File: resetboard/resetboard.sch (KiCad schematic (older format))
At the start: 24 parts, among them J1 USB_C_Receptacle_USB2.0, J2 Conn_02x20_Odd_Even, J3 Conn_01x02, J4 Conn_01x06, SW1 SW_SPST, U1 PCF8523TK, U2 SE050, Y1 Crystal_Small

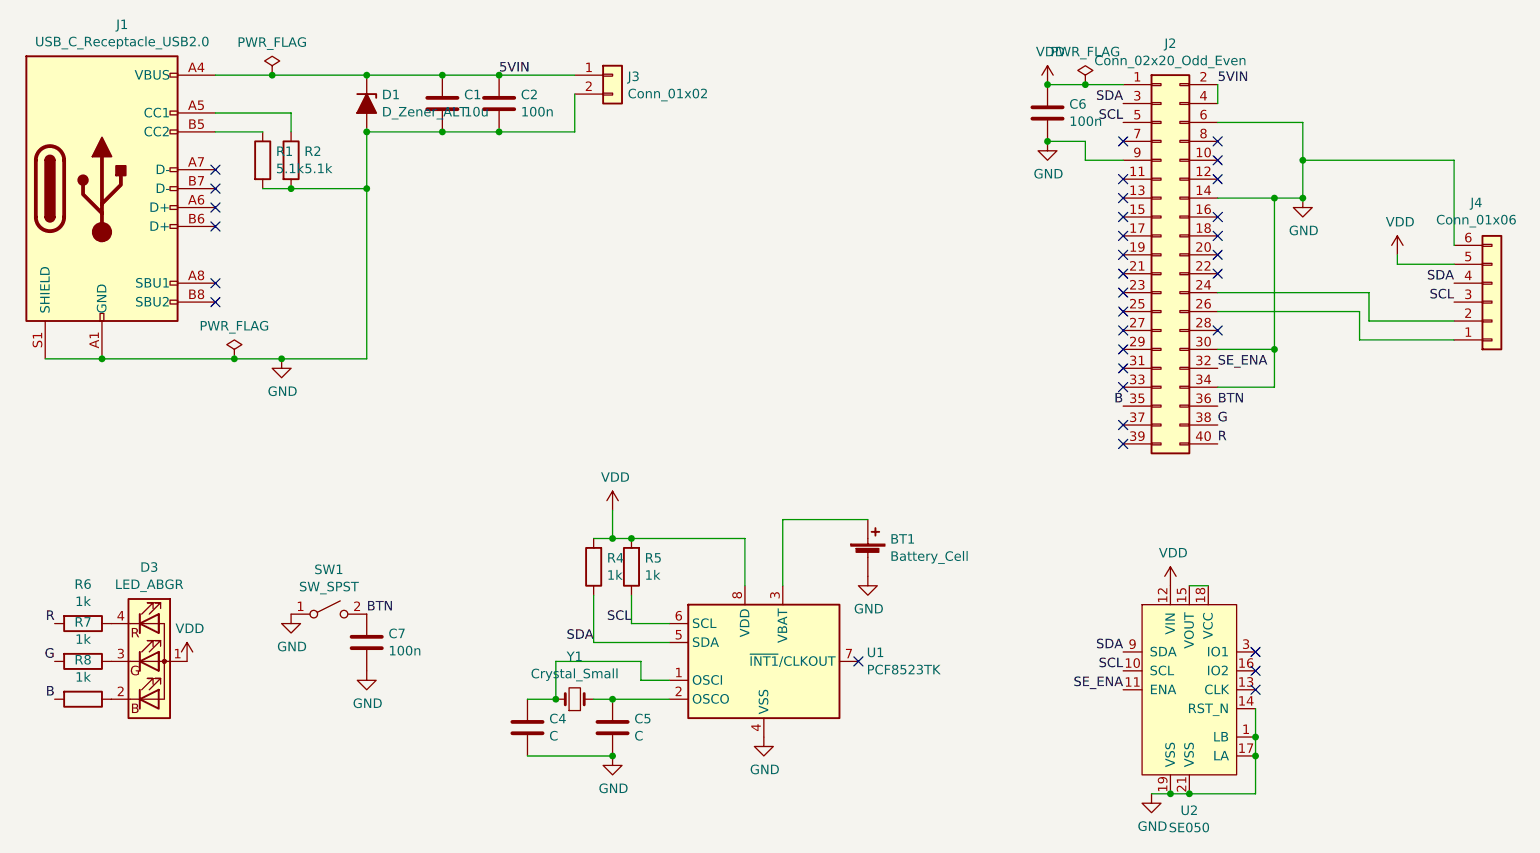
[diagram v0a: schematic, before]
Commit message: Remove ziptie holes Add filtering to RTC supply Add NFET-controlled fan on GPIO18 Switch fan connector to horizontal Rearrange parts to move fan connector to left edge of board Rotate LED towards edge Relabel R and B channels of RGB LED to match part Add vendor STEP model for RGB LED Regenerate STEP file
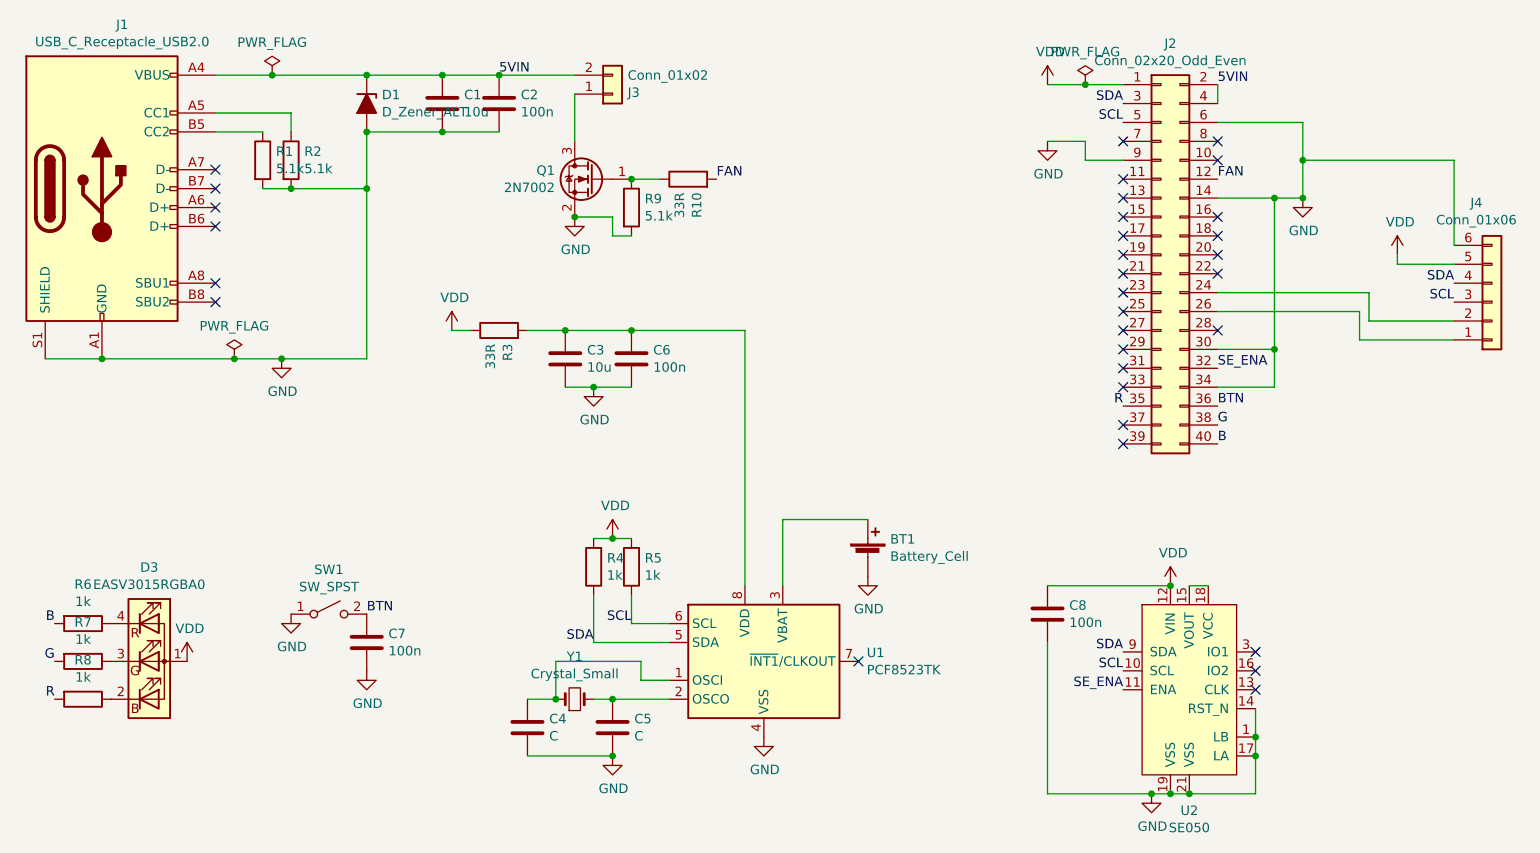
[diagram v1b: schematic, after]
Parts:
- added C3: 10u, Capacitor_SMD:C_0805_2012Metric, symbol Device:C
- added C8: 100n, Capacitor_SMD:C_0603_1608Metric, symbol Device:C
- added Q1: 2N7002, Package_TO_SOT_SMD:SOT-23, symbol Transistor_FET:2N7002
- added R10, R3: 33R, Resistor_SMD:R_0603_1608Metric, symbol Device:R
- added R9: 5.1k, Resistor_SMD:R_0603_1608Metric, symbol Device:R
- D3: value LED_ABGR -> EASV3015RGBA0
- J3: footprint Connector_JST:JST_GH_BM02B-GHS-TBT_1x02-1MP_P1.25mm_Vertical -> Connector_JST:JST_GH_SM02B-GHS-TB_1x02-1MP_P1.25mm_Horizontal
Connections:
- net 5VIN: now also J3.2 (Pin_2); no longer J3.1 (Pin_1)
- net B: now also J2.40 (Pin_40), R6.2; no longer J2.35 (Pin_35), R8.2
- net GND: now also C3.2, C8.2, Q1.2 (S), R9.2; no longer J3.2 (Pin_2)
- net R: now also J2.35 (Pin_35), R8.2; no longer J2.40 (Pin_40), R6.2
- net VDD: now also C8.1, R3.1; no longer C6.1, U1.8 (VDD)
- net FAN: now reaches J2.12 (Pin_12)
- net FAN: now also R10.2
- new net: C3.1, C6.1, R3.2, U1.8 (VDD)
- new net: J3.1 (Pin_1), Q1.3 (D)
- new net: Q1.1 (G), R10.1, R9.1
- no-connect marks 33 -> 32
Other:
- moved on the sheet: C6
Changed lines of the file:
@@
 P 3100 5300
 F 0 "D3" H 3100 5797 50  0000 C CNN
-F 1 "LED_ABGR" H 3100 5706 50  0000 C CNN
+F 1 "EASV3015RGBA0" H 3100 5706 50  0000 C CNN
 F 2 "catwsparts:HQ12-2353RBGC" H 3100 5250 50  0001 C CNN
 F 3 "~" H 3100 5250 50  0001 C CNN
@@
 Wire Wire Line
 	5450 5200 5450 4950
-Wire Wire Line
-	5450 4650 5550 4650
-Connection ~ 5550 4650
-Wire Wire Line
-	5550 4650 5650 4650
-$Comp
-L power:VDD #PWR0103
-U 1 1 5FC4EE71
-P 5550 4500
-F 0 "#PWR0103" H 5550 4350 50  0001 C CNN
-F 1 "VDD" H 5565 4673 50  0000 C CNN
-F 2 "" H 5550 4500 50  0001 C CNN
-F 3 "" H 5550 4500 50  0001 C CNN
-	1    5550 4500
-	1    0    0    -1
-$EndComp
 $Comp
 L power:VDD #PWR0104
@@
 $EndComp
 Connection ~ 9200 2850
-Text Label 8750 4150 0    50   ~ 0
+Text Label 8250 3950 2    50   ~ 0
 R
 Text Label 8750 4050 0    50   ~ 0
 G
-Text Label 8250 3950 2    50   ~ 0
+Text Label 8750 4150 0    50   ~ 0
 B
 $Comp
@@
 Text Label 4250 5050 0    50   ~ 0
 BTN
-Text Label 2600 5100 2    50   ~ 0
+Text Label 2600 5500 2    50   ~ 0
 R
 Text Label 2600 5300 2    50   ~ 0
 G
-Text Label 2600 5500 2    50   ~ 0
+Text Label 2600 5100 2    50   ~ 0
 B
 $Comp
@@
 SE_ENA
 Wire Wire Line
-	5650 4650 6250 4650
-Wire Wire Line
-	6250 4650 6250 4900
-Connection ~ 5650 4650
-Wire Wire Line
 	6450 4550 6450 4900
 $Comp
@@
 NoConn ~ 8750 2550
 NoConn ~ 8750 2650
-NoConn ~ 8750 2750
 NoConn ~ 8250 3050
 NoConn ~ 8250 3150
@@
 L Device:C C6
 U 1 1 5FCBB4FA
-P 7850 2400
-F 0 "C6" H 7965 2446 50  0000 L CNN
-F 1 "100n" H 7965 2355 50  0000 L CNN
-F 2 "Capacitor_SMD:C_0603_1608Metric" H 7888 2250 50  0001 C CNN
-F 3 "~" H 7850 2400 50  0001 C CNN
-	1    7850 2400
-	1    0    0    -1
-$EndComp
-Connection ~ 7850 2250
+P 5650 3700
+F 0 "C6" H 5765 3746 50  0000 L CNN
+F 1 "100n" H 5765 3655 50  0000 L CNN
+F 2 "Capacitor_SMD:C_0603_1608Metric" H 5688 3550 50  0001 C CNN
+F 3 "~" H 5650 3700 50  0001 C CNN
+	1    5650 3700
+	1    0    0    -1
+$EndComp
 $Comp
 L power:GND #PWR0109
@@
 Wire Wire Line
 	8050 2550 7850 2550
-Connection ~ 7850 2550
 NoConn ~ 8250 2750
 NoConn ~ 8250 2850
@@
 NoConn ~ 8750 2950
 NoConn ~ 8750 3050
-Wire Wire Line
-	5550 4500 5550 4650
 $Comp
 L Device:Battery_Cell BT1
@@
 L Connector_Generic:Conn_01x02 J3
 U 1 1 5FCF28DB
-P 5550 2200
-F 0 "J3" H 5630 2192 50  0000 L CNN
-F 1 "Conn_01x02" H 5630 2101 50  0000 L CNN
-F 2 "Connector_JST:JST_GH_BM02B-GHS-TBT_1x02-1MP_P1.25mm_Vertical" H 5550 2200 50  0001 C CNN
-F 3 "~" H 5550 2200 50  0001 C CNN
-	1    5550 2200
-	1    0    0    -1
+P 5550 2300
+F 0 "J3" H 5630 2292 50  0000 L CNN
+F 1 "Conn_01x02" H 5630 2201 50  0000 L CNN
+F 2 "Connector_JST:JST_GH_SM02B-GHS-TB_1x02-1MP_P1.25mm_Horizontal" H 5550 2300 50  0001 C CNN
+F 3 "~" H 5550 2300 50  0001 C CNN
+	1    5550 2300
+	1    0    0    1
 $EndComp
 Wire Wire Line
 	5350 2200 4950 2200
 Connection ~ 4950 2200
-Wire Wire Line
-	4950 2500 5350 2500
-Wire Wire Line
-	5350 2500 5350 2300
-Connection ~ 4950 2500
 $Comp
 L Connector_Generic:Conn_01x06 J4
@@
 Wire Wire Line
 	9700 3200 9700 3150
+$Comp
+L Device:C C3
+U 1 1 603513FE
+P 5300 3700
+F 0 "C3" H 5415 3746 50  0000 L CNN
+F 1 "10u" H 5415 3655 50  0000 L CNN
+F 2 "Capacitor_SMD:C_0805_2012Metric" H 5338 3550 50  0001 C CNN
+F 3 "~" H 5300 3700 50  0001 C CNN
+	1    5300 3700
+	1    0    0    -1
+$EndComp
+$Comp
+L Device:R R3
+U 1 1 6035DB2C
+P 4950 3550
+F 0 "R3" H 4880 3504 50  0000 R CNN
+F 1 "33R" H 4880 3595 50  0000 R CNN
+F 2 "Resistor_SMD:R_0603_1608Metric" V 4880 3550 50  0001 C CNN
+F 3 "~" H 4950 3550 50  0001 C CNN
+	1    4950 3550
+	0    -1   -1   0
+$EndComp
+$Comp
+L power:VDD #PWR0103
+U 1 1 6035F8DB
+P 4700 3550
+F 0 "#PWR0103" H 4700 3400 50  0001 C CNN
+F 1 "VDD" H 4715 3723 50  0000 C CNN
+F 2 "" H 4700 3550 50  0001 C CNN
+F 3 "" H 4700 3550 50  0001 C CNN
+	1    4700 3550
+	1    0    0    -1
+$EndComp
+Wire Wire Line
+	4700 3550 4800 3550
+Wire Wire Line
+	5100 3550 5300 3550
+Wire Wire Line
+	5300 3550 5650 3550
+Connection ~ 5300 3550
+Wire Wire Line
+	5300 3850 5450 3850
+$Comp
+L power:GND #PWR0115
+U 1 1 60367D9C
+P 5450 3850
+F 0 "#PWR0115" H 5450 3600 50  0001 C CNN
+F 1 "GND" H 5455 3677 50  0000 C CNN
+F 2 "" H 5450 3850 50  0001 C CNN
+F 3 "" H 5450 3850 50  0001 C CNN
+	1    5450 3850
+	1    0    0    -1
+$EndComp
+Connection ~ 5450 3850
+Wire Wire Line
+	5450 3850 5650 3850
+Wire Wire Line
+	5650 3550 6250 3550
+Connection ~ 5650 3550
+$Comp
+L Device:C C8
+U 1 1 6036A59B
+P 7850 5050
+F 0 "C8" H 7965 5096 50  0000 L CNN
+F 1 "100n" H 7965 5005 50  0000 L CNN
+F 2 "Capacitor_SMD:C_0603_1608Metric" H 7888 4900 50  0001 C CNN
+F 3 "~" H 7850 5050 50  0001 C CNN
+	1    7850 5050
+	1    0    0    -1
+$EndComp
+Wire Wire Line
+	8500 4900 7850 4900
+Connection ~ 8500 4900
+Wire Wire Line
+	7850 5200 7850 6000
+Wire Wire Line
+	7850 6000 8400 6000
+Connection ~ 8400 6000
+$Comp
+L Transistor_FET:2N7002 Q1
+U 1 1 6037907E
+P 5450 2750
+F 0 "Q1" H 5655 2796 50  0000 L CNN
+F 1 "2N7002" H 5655 2705 50  0000 L CNN
+F 2 "Package_TO_SOT_SMD:SOT-23" H 5650 2675 50  0001 L CIN
+F 3 "" H 5450 2750 50  0001 L CNN
+	1    5450 2750
+	-1   0    0    -1
+$EndComp
+Wire Wire Line
+	5350 2300 5350 2550
+$Comp
+L power:GND #PWR0116
+U 1 1 60383F33
+P 5350 2950
+F 0 "#PWR0116" H 5350 2700 50  0001 C CNN
+F 1 "GND" H 5355 2777 50  0000 C CNN
+F 2 "" H 5350 2950 50  0001 C CNN
+F 3 "" H 5350 2950 50  0001 C CNN
+	1    5350 2950
+	1    0    0    -1
+$EndComp
+$Comp
+L Device:R R9
+U 1 1 603884B5
+P 5650 2900
+F 0 "R9" H 5720 2946 50  0000 L CNN
+F 1 "5.1k" H 5720 2855 50  0000 L CNN
+F 2 "Resistor_SMD:R_0603_1608Metric" V 5580 2900 50  0001 C CNN
+F 3 "~" H 5650 2900 50  0001 C CNN
+	1    5650 2900
+	1    0    0    -1
+$EndComp
+Wire Wire Line
+	5350 2950 5550 2950
+Wire Wire Line
+	5550 2950 5550 3050
+Wire Wire Line
+	5550 3050 5650 3050
+Connection ~ 5350 2950
+$Comp
+L Device:R R10
+U 1 1 6038CCDB
+P 5950 2750
+F 0 "R10" H 5880 2704 50  0000 R CNN
+F 1 "33R" H 5880 2795 50  0000 R CNN
+F 2 "Resistor_SMD:R_0603_1608Metric" V 5880 2750 50  0001 C CNN
+F 3 "~" H 5950 2750 50  0001 C CNN
+	1    5950 2750
+	0    -1   -1   0
+$EndComp
+Wire Wire Line
+	5800 2750 5650 2750
+Connection ~ 5650 2750
+Text Label 6100 2750 0    50   ~ 0
+FAN
+Text Label 8750 2750 0    50   ~ 0
+FAN
+Wire Wire Line
+	5450 4650 5550 4650
+Wire Wire Line
+	6250 3550 6250 4900
+$Comp
+L power:VDD #PWR0117
+U 1 1 603B7B40
+P 5550 4650
+F 0 "#PWR0117" H 5550 4500 50  0001 C CNN
+F 1 "VDD" H 5565 4823 50  0000 C CNN
+F 2 "" H 5550 4650 50  0001 C CNN
+F 3 "" H 5550 4650 50  0001 C CNN
+	1    5550 4650
+	1    0    0    -1
+$EndComp
+Connection ~ 5550 4650
+Wire Wire Line
+	5550 4650 5650 4650
 $EndSCHEMATC
